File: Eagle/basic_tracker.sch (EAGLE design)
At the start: 21 parts, among them CN1 BATTERY, IC1 MCP1700 3.3v, X1 SMA

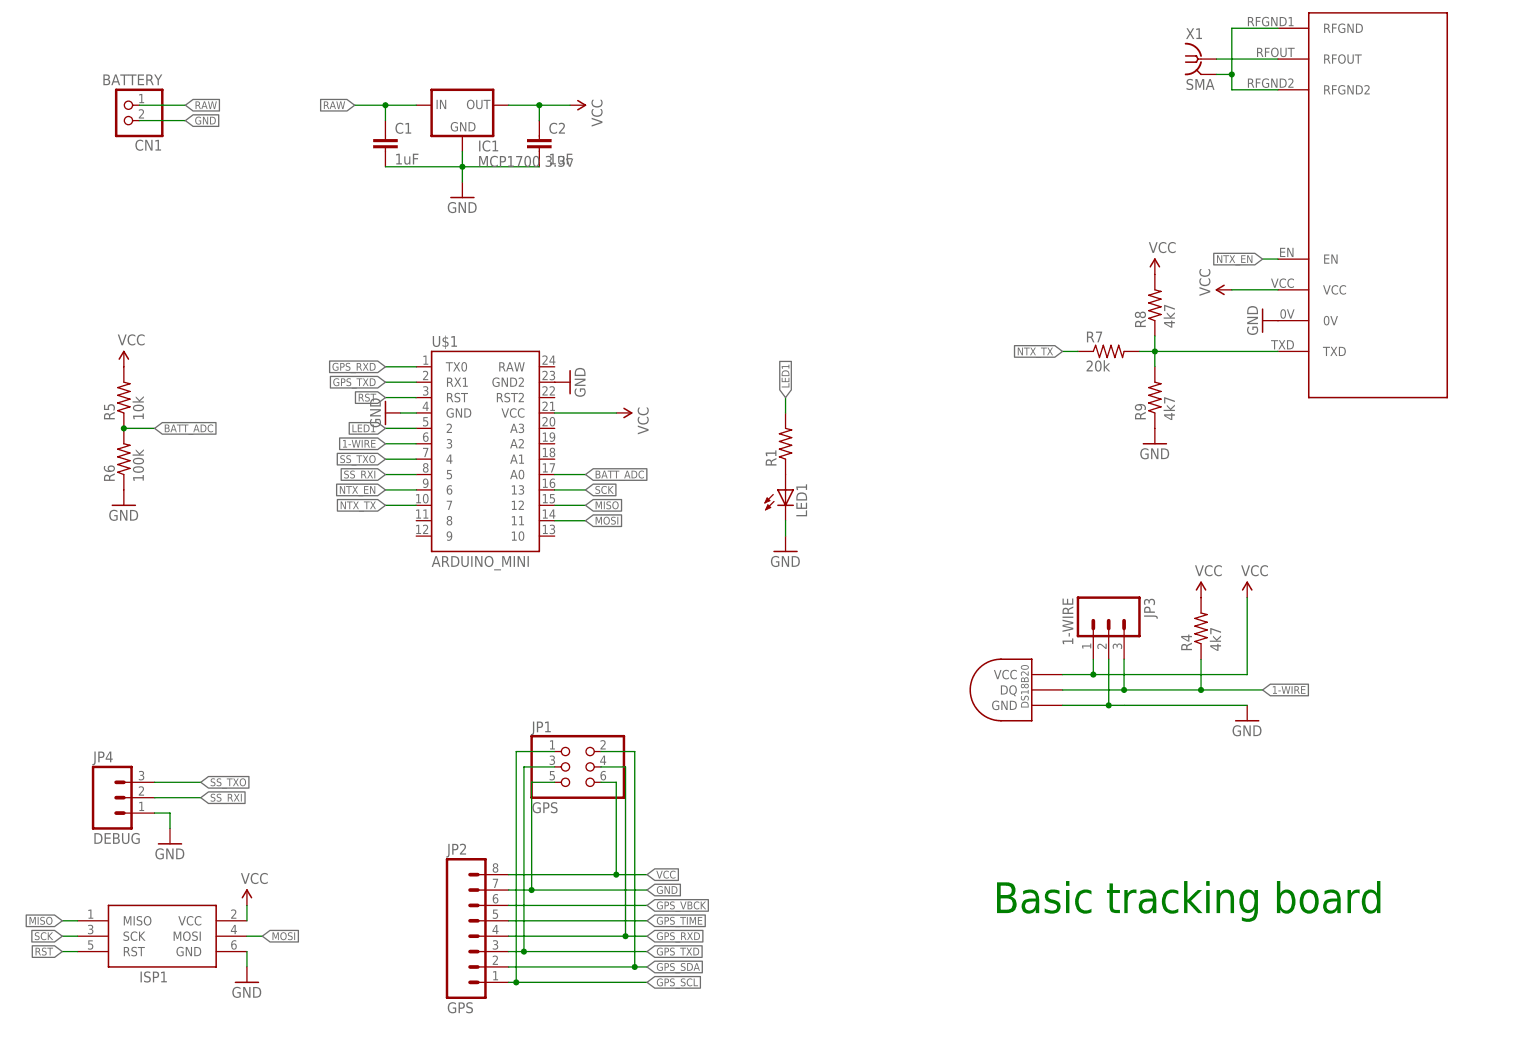
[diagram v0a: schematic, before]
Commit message: Updated board text and cap sizes
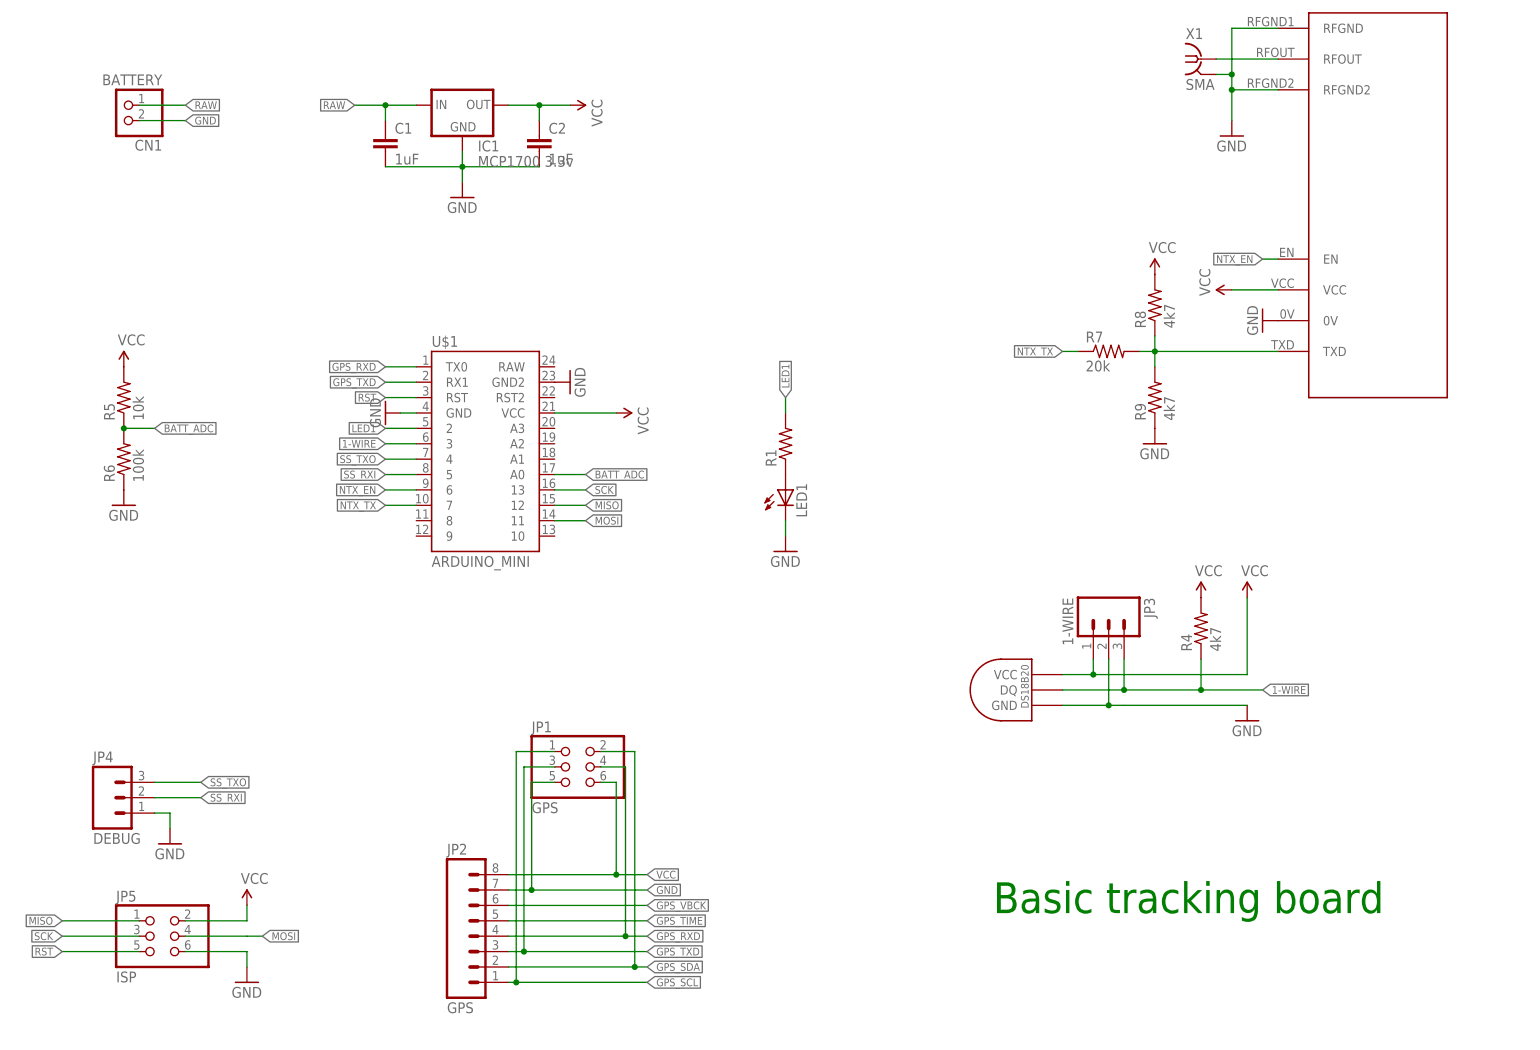
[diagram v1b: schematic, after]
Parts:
- removed ISP1: AVRISP-6, adafruit:AVRISP-6
- added JP5: ISP, SparkFun:PINHD-2X3
- C1, C2: device SparkFun:CAPPTH -> SparkFun:CAPPTH1
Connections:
- removed net N$5: U$3.RFGND, U$3.RFGND2, X1G$1.GND
- net GND: now also JP5.6, U$3.RFGND, U$3.RFGND2, X1G$1.GND; no longer ISP1.GND
- net MISO: now also JP5.1; no longer ISP1.MISO
- net MOSI: now also JP5.4; no longer ISP1.MOSI
- net RST: now also JP5.5; no longer ISP1.RST
- net SCK: now also JP5.3; no longer ISP1.SCK
- net VCC: now also JP5.2; no longer ISP1.VCC
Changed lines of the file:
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@@
 <part name="JP1" library="SparkFun" deviceset="PINHD-2X3" device="" value="GPS"/>
 <part name="U$2" library="Ava" deviceset="DS1820" device="TO92"/>
-<part name="ISP1" library="adafruit" deviceset="AVRISP" device="-6"/>
 <part name="CN1" library="adafruit" deviceset="JST_2PIN" device="-THM-RA" value="BATTERY"/>
 <part name="IC1" library="adafruit" deviceset="MCP1700" device="INLINE" value="MCP1700 3.3v"/>
@@
 <part name="LED1" library="SparkFun" deviceset="LED" device="3MM"/>
 <part name="JP2" library="SparkFun" deviceset="M08" device="1X08" value="GPS"/>
-<part name="C1" library="SparkFun" deviceset="CAP" device="PTH" value="1uF"/>
-<part name="C2" library="SparkFun" deviceset="CAP" device="PTH" value="1uF"/>
+<part name="C1" library="SparkFun" deviceset="CAP" device="PTH1" value="1uF"/>
+<part name="C2" library="SparkFun" deviceset="CAP" device="PTH1" value="1uF"/>
 <part name="FRAME1" library="frames" deviceset="DINA4_L" device=""/>
+<part name="JP5" library="SparkFun" deviceset="PINHD-2X3" device="" value="ISP"/>
+<part name="GND11" library="SparkFun" deviceset="GND" device=""/>
 </parts>
 <sheets>
@@
 <instance part="JP1" gate="A" x="111.76" y="50.8"/>
 <instance part="U$2" gate="G$1" x="187.96" y="63.5" rot="R90"/>
-<instance part="ISP1" gate="G$1" x="43.18" y="22.86"/>
 <instance part="CN1" gate="G$1" x="38.1" y="160.02" rot="R180"/>
 <instance part="IC1" gate="1" x="93.98" y="160.02"/>
@@
 <instance part="FRAME1" gate="G$1" x="0" y="0"/>
 <instance part="FRAME1" gate="G$2" x="162.56" y="0"/>
+<instance part="JP5" gate="A" x="43.18" y="22.86"/>
+<instance part="GND11" gate="1" x="220.98" y="154.94"/>
 </instances>
 <busses>
@@
 </segment>
 <segment>
-<pinref part="ISP1" gate="G$1" pin="VCC"/>
 <pinref part="P+6" gate="1" pin="VCC"/>
 <wire x1="58.42" y1="27.94" x2="58.42" y2="25.4" width="0.1524" layer="91"/>
+<pinref part="JP5" gate="A" pin="2"/>
+<wire x1="48.26" y1="25.4" x2="58.42" y2="25.4" width="0.1524" layer="91"/>
 </segment>
 <segment>
@@
 </segment>
 <segment>
-<pinref part="ISP1" gate="G$1" pin="GND"/>
 <pinref part="GND4" gate="1" pin="GND"/>
 <wire x1="58.42" y1="17.78" x2="58.42" y2="20.32" width="0.1524" layer="91"/>
+<pinref part="JP5" gate="A" pin="6"/>
+<wire x1="48.26" y1="20.32" x2="58.42" y2="20.32" width="0.1524" layer="91"/>
 </segment>
 <segment>
@@
 <wire x1="40.64" y1="157.48" x2="48.26" y2="157.48" width="0.1524" layer="91"/>
 <label x="48.26" y="157.48" size="1.27" layer="95" xref="yes"/>
+</segment>
+<segment>
+<pinref part="X1" gate="G$1" pin="GND"/>
+<wire x1="218.44" y1="165.1" x2="220.98" y2="165.1" width="0.1524" layer="91"/>
+<wire x1="220.98" y1="165.1" x2="220.98" y2="162.56" width="0.1524" layer="91"/>
+<pinref part="U$3" gate="G$1" pin="RFGND2"/>
+<wire x1="220.98" y1="162.56" x2="228.6" y2="162.56" width="0.1524" layer="91"/>
+<wire x1="220.98" y1="165.1" x2="220.98" y2="172.72" width="0.1524" layer="91"/>
+<junction x="220.98" y="165.1"/>
+<pinref part="U$3" gate="G$1" pin="RFGND"/>
+<wire x1="220.98" y1="172.72" x2="228.6" y2="172.72" width="0.1524" layer="91"/>
+<pinref part="GND11" gate="1" pin="GND"/>
+<wire x1="220.98" y1="157.48" x2="220.98" y2="162.56" width="0.1524" layer="91"/>
+<junction x="220.98" y="162.56"/>
 </segment>
 </net>
@@
 </segment>
 </net>
-<net name="N$5" class="0">
-<segment>
-<pinref part="X1" gate="G$1" pin="GND"/>
-<wire x1="218.44" y1="165.1" x2="220.98" y2="165.1" width="0.1524" layer="91"/>
-<wire x1="220.98" y1="165.1" x2="220.98" y2="162.56" width="0.1524" layer="91"/>
-<pinref part="U$3" gate="G$1" pin="RFGND2"/>
-<wire x1="220.98" y1="162.56" x2="228.6" y2="162.56" width="0.1524" layer="91"/>
-<wire x1="220.98" y1="165.1" x2="220.98" y2="172.72" width="0.1524" layer="91"/>
-<junction x="220.98" y="165.1"/>
-<pinref part="U$3" gate="G$1" pin="RFGND"/>
-<wire x1="220.98" y1="172.72" x2="228.6" y2="172.72" width="0.1524" layer="91"/>
-</segment>
-</net>
 <net name="N$6" class="0">
 <segment>
@@
 <net name="MOSI" class="0">
 <segment>
-<pinref part="ISP1" gate="G$1" pin="MOSI"/>
 <wire x1="58.42" y1="22.86" x2="60.96" y2="22.86" width="0.1524" layer="91"/>
 <label x="60.96" y="22.86" size="1.27" layer="95" xref="yes"/>
+<pinref part="JP5" gate="A" pin="4"/>
+<wire x1="48.26" y1="22.86" x2="58.42" y2="22.86" width="0.1524" layer="91"/>
 </segment>
 <segment>
@@
 <net name="MISO" class="0">
 <segment>
-<pinref part="ISP1" gate="G$1" pin="MISO"/>
-<wire x1="30.48" y1="25.4" x2="27.94" y2="25.4" width="0.1524" layer="91"/>
+<wire x1="40.64" y1="25.4" x2="27.94" y2="25.4" width="0.1524" layer="91"/>
 <label x="27.94" y="25.4" size="1.27" layer="95" rot="R180" xref="yes"/>
+<pinref part="JP5" gate="A" pin="1"/>
 </segment>
 <segment>
@@
 <net name="SCK" class="0">
 <segment>
-<pinref part="ISP1" gate="G$1" pin="SCK"/>
-<wire x1="30.48" y1="22.86" x2="27.94" y2="22.86" width="0.1524" layer="91"/>
+<wire x1="40.64" y1="22.86" x2="27.94" y2="22.86" width="0.1524" layer="91"/>
 <label x="27.94" y="22.86" size="1.27" layer="95" rot="R180" xref="yes"/>
+<pinref part="JP5" gate="A" pin="3"/>
 </segment>
 <segment>
@@
 <net name="RST" class="0">
 <segment>
-<pinref part="ISP1" gate="G$1" pin="RST"/>
-<wire x1="30.48" y1="20.32" x2="27.94" y2="20.32" width="0.1524" layer="91"/>
+<wire x1="40.64" y1="20.32" x2="27.94" y2="20.32" width="0.1524" layer="91"/>
 <label x="27.94" y="20.32" size="1.27" layer="95" rot="R180" xref="yes"/>
-</segment>
-<segment>
+<pinref part="JP5" gate="A" pin="5"/>
+</segment>
+<segment>
